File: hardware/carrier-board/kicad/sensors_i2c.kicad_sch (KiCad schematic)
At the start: 0 parts

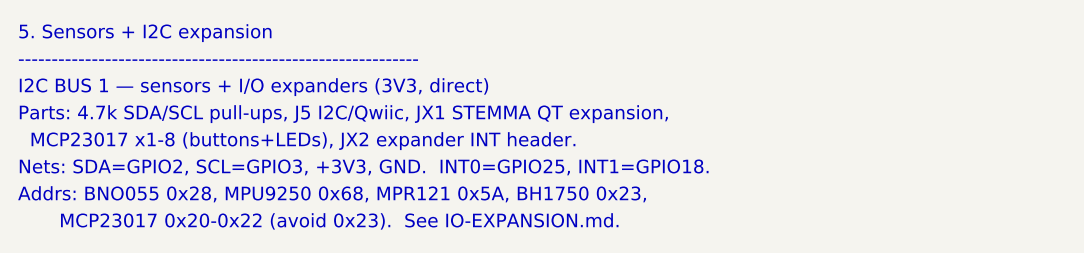
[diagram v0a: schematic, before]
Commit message: Carrier docs + KiCad plan: full two-brain pass (CM5 HUB75 + RP2354B I/O)
Propagate the two-brain architecture across the whole doc set and KiCad plan:
- REQUIREMENTS: restructured M1-M12 (CM5 HUB75; RP2354B core/MAX7219/WS2812/
  sensors/buttons/servos; USB selector + standalone program port); N-list reworked.
- POWER: add +V_SERVO and +3V3_RP rails, servo current budget, updated worked
  total + protection; sensors now on +3V3_RP not CM5 3V3.
- CONNECTORS: J3 re-sourced to RP2354B SPI0, J4 4 WS2812 zones, J5 +SENS_INT,
  J6 BTN1..10, add J12 USB-C, J20-J27 servos, SW1 USB selector, SWD/UART hdrs;
  drop JP1/JP2; fans presented as RP2354B-default-or-CM5 (decision flagged).
- BOM: add RP2354B core, '125/'245 (RP side), USB mux/USB-C/ESD, servo headers,
  +3V3_RP reg; fix '125 double-count and stale HUB75/MAX7219-shared-buffer/JP1.
- MULTI-BACKEND: HUB75+MAX7219 now simultaneous (different brains); firmware
  CompositePanelOutput is the sole remaining blocker.
- IO-EXPANSION: RP2354B is the primary I/O backbone; I2C expanders secondary.
- kicad: 11-sheet plan, stable UUIDs, generator skips populated face_buffer.
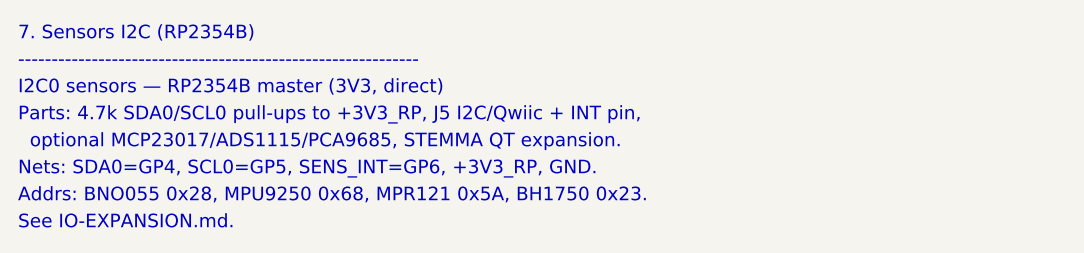
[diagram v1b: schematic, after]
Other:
- note added: "7. Sensors I2C (RP2354B)"
- note added: "Addrs: BNO055 0x28, MPU9250 0x68, MPR121 0x5A, BH1750 0x23."
- note added: "I2C0 sensors — RP2354B master (3V3, direct)"
- note added: "Nets: SDA0=GP4, SCL0=GP5, SENS_INT=GP6, +3V3_RP, GND."
- note added: "Parts: 4.7k SDA0/SCL0 pull-ups to +3V3_RP, J5 I2C/Qwiic + INT pin,"
- note added: "See IO-EXPANSION.md."
- note added: "optional MCP23017/ADS1115/PCA9685, STEMMA QT expansion."
- note removed: "5. Sensors + I2C expansion"
- note removed: "Addrs: BNO055 0x28, MPU9250 0x68, MPR121 0x5A, BH1750 0x23,"
- note removed: "I2C BUS 1 — sensors + I/O expanders (3V3, direct)"
- note removed: "MCP23017 0x20-0x22 (avoid 0x23). See IO-EXPANSION.md."
- note removed: "MCP23017 x1-8 (buttons+LEDs), JX2 expander INT header."
- note removed: "Nets: SDA=GPIO2, SCL=GPIO3, +3V3, GND. INT0=GPIO25, INT1=GPIO18."
- note removed: "Parts: 4.7k SDA/SCL pull-ups, J5 I2C/Qwiic, JX1 STEMMA QT expansion,"
- title: ProtoHUD Carrier — 5. Sensors + I2C expansion -> ProtoHUD Carrier — 7. Sensors I2C (RP2354B)
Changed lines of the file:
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@@
   (paper "A3")
   (title_block
-    (title "ProtoHUD Carrier — 5. Sensors + I2C expansion")
+    (title "ProtoHUD Carrier — 7. Sensors I2C (RP2354B)")
     (rev "A")
     (company "ProtoHUD")
   )
-  (text "5. Sensors + I2C expansion" (at 25.4 25.40 0) (effects (font (size 1.5 1.5)) (justify left bottom)))
+  (text "7. Sensors I2C (RP2354B)" (at 25.4 25.40 0) (effects (font (size 1.5 1.5)) (justify left bottom)))
   (text "------------------------------------------------------------" (at 25.4 28.40 0) (effects (font (size 1.5 1.5)) (justify left bottom)))
-  (text "I2C BUS 1 — sensors + I/O expanders (3V3, direct)" (at 25.4 31.40 0) (effects (font (size 1.5 1.5)) (justify left bottom)))
-  (text "Parts: 4.7k SDA/SCL pull-ups, J5 I2C/Qwiic, JX1 STEMMA QT expansion," (at 25.4 34.40 0) (effects (font (size 1.5 1.5)) (justify left bottom)))
-  (text "  MCP23017 x1-8 (buttons+LEDs), JX2 expander INT header." (at 25.4 37.40 0) (effects (font (size 1.5 1.5)) (justify left bottom)))
-  (text "Nets: SDA=GPIO2, SCL=GPIO3, +3V3, GND.  INT0=GPIO25, INT1=GPIO18." (at 25.4 40.40 0) (effects (font (size 1.5 1.5)) (justify left bottom)))
-  (text "Addrs: BNO055 0x28, MPU9250 0x68, MPR121 0x5A, BH1750 0x23," (at 25.4 43.40 0) (effects (font (size 1.5 1.5)) (justify left bottom)))
-  (text "       MCP23017 0x20-0x22 (avoid 0x23).  See IO-EXPANSION.md." (at 25.4 46.40 0) (effects (font (size 1.5 1.5)) (justify left bottom)))
+  (text "I2C0 sensors — RP2354B master (3V3, direct)" (at 25.4 31.40 0) (effects (font (size 1.5 1.5)) (justify left bottom)))
+  (text "Parts: 4.7k SDA0/SCL0 pull-ups to +3V3_RP, J5 I2C/Qwiic + INT pin," (at 25.4 34.40 0) (effects (font (size 1.5 1.5)) (justify left bottom)))
+  (text "  optional MCP23017/ADS1115/PCA9685, STEMMA QT expansion." (at 25.4 37.40 0) (effects (font (size 1.5 1.5)) (justify left bottom)))
+  (text "Nets: SDA0=GP4, SCL0=GP5, SENS_INT=GP6, +3V3_RP, GND." (at 25.4 40.40 0) (effects (font (size 1.5 1.5)) (justify left bottom)))
+  (text "Addrs: BNO055 0x28, MPU9250 0x68, MPR121 0x5A, BH1750 0x23." (at 25.4 43.40 0) (effects (font (size 1.5 1.5)) (justify left bottom)))
+  (text "See IO-EXPANSION.md." (at 25.4 46.40 0) (effects (font (size 1.5 1.5)) (justify left bottom)))
   (sheet_instances
     (path "/" (page "1"))

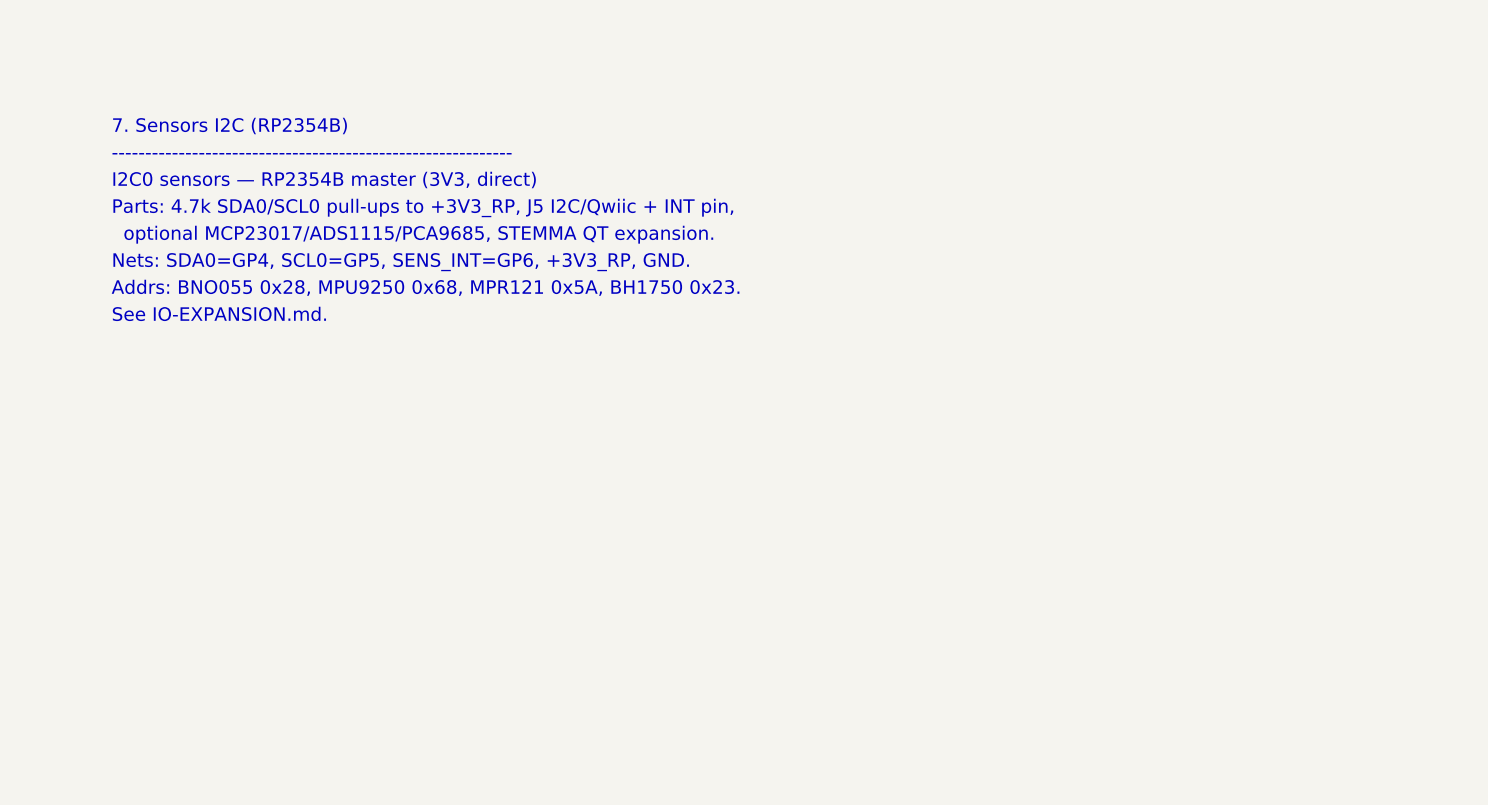
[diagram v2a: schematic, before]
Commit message: Carrier KiCad: populate all 11 schematic sheets
Replace populate_face_buffer.py with populate_sheets.py: one generator that
emits all 11 populated sub-sheets reusing the KiCad-9 format proven by the
face_buffer proof. Shared symbol library + generic box-symbol builder; condensed
CM5 (2x DF40-100) and RP2354B (QFN-80) symbols showing only used pins.

Connectivity by net labels (global for rails + cross-sheet nets: GPIOxx HUB75,
MX_*, LED*_DAT, SRV*, BTN*, *_USB_*; local within-sheet). Sheets: power
(protection + rails + AP2112 +3V3_RP), cm5 (HUB75 out + fan MOSFETs + RP ctrl),
face_buffer, rp2354_io (RP2354B + xtal + SW1/J12 + ESD + SWD), rp2354_face
(U10->J3), leds (U11 quad ->J4a-d), sensors_i2c (pull-ups+J5+STEMMA),
servos (J20-27 + rail), gpio_buttons (J6), usb (USB2514B hub + uplink),
cameras_display (CSI FFC + HDMI).

Verified: all sheets paren-balanced, every used lib_id defined, all instance
paths match sheet UUIDs, root<->sub-sheet UUID linkage intact. generate_skeleton.py
now lists all sheets POPULATED (writes only root+project). Not yet opened in
KiCad here -- expect ERC warnings (PWR_FLAG, unconnected pins) to clean.
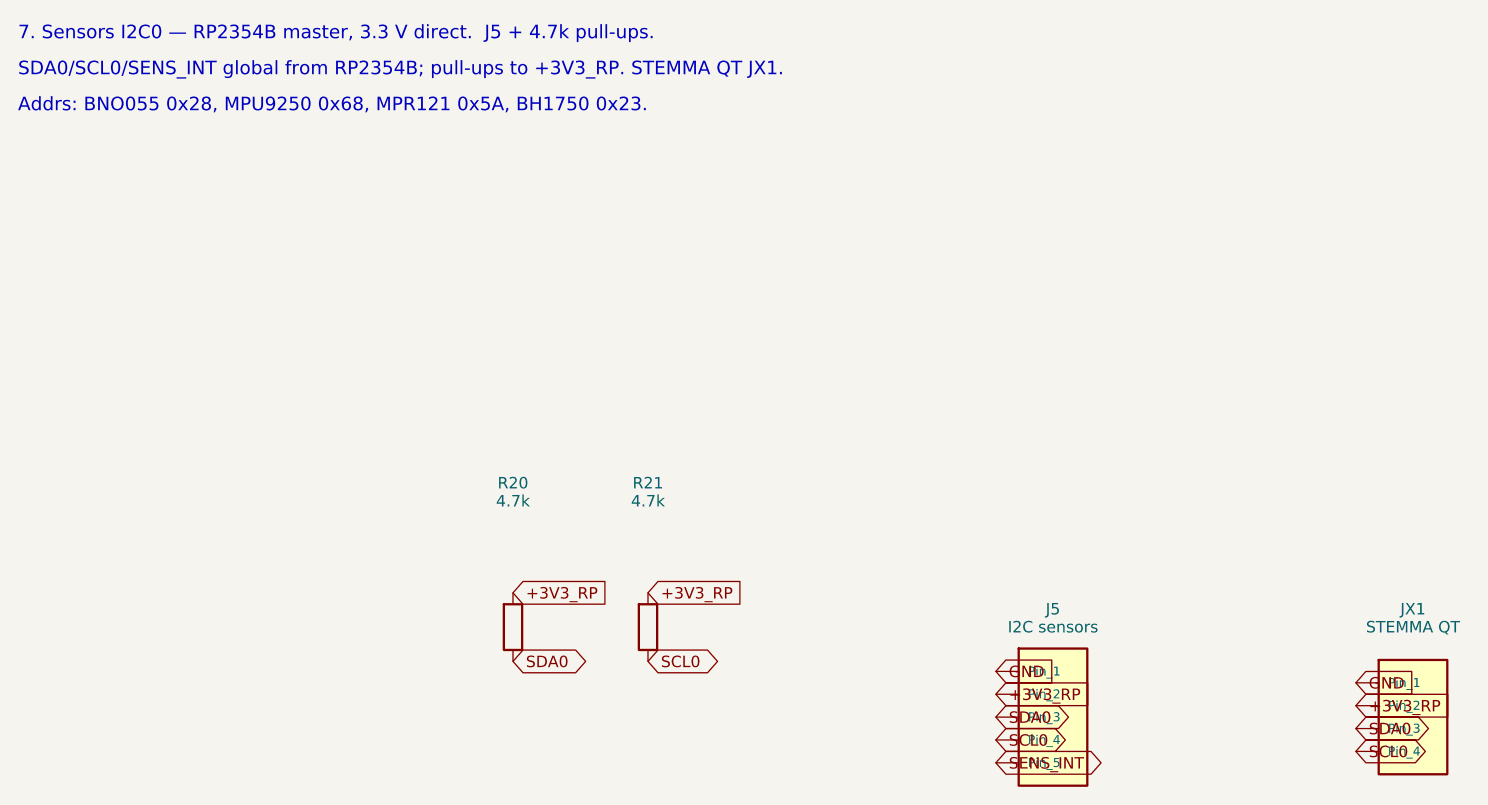
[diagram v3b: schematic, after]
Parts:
- added J5: I2C sensors, symbol Connector_Generic:Conn_01x05
- added JX1: STEMMA QT, symbol Connector_Generic:Conn_01x04
- added R20, R21: 4.7k, symbol Device:R
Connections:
- new net +3V3_RP: J5.2 (Pin_2), JX1.2 (Pin_2), R20.1, R21.1
- new net GND: J5.1 (Pin_1), JX1.1 (Pin_1)
- new net SCL0: J5.4 (Pin_4), JX1.4 (Pin_4), R21.2
- new net SDA0: J5.3 (Pin_3), JX1.3 (Pin_3), R20.2
- new net SENS_INT: J5.5 (Pin_5)
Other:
- note added: "7. Sensors I2C0 — RP2354B master, 3.3 V direct. J5 + 4.7k pull-ups."
- note added: "SDA0/SCL0/SENS_INT global from RP2354B; pull-ups to +3V3_RP. STEMMA QT JX1."
- note removed: "------------------------------------------------------------"
- note removed: "7. Sensors I2C (RP2354B)"
- note removed: "I2C0 sensors — RP2354B master (3V3, direct)"
- note removed: "Nets: SDA0=GP4, SCL0=GP5, SENS_INT=GP6, +3V3_RP, GND."
- note removed: "Parts: 4.7k SDA0/SCL0 pull-ups to +3V3_RP, J5 I2C/Qwiic + INT pin,"
- note removed: "See IO-EXPANSION.md."
- note removed: "optional MCP23017/ADS1115/PCA9685, STEMMA QT expansion."
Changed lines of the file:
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@@
 (kicad_sch
-  (version 20230121)
-  (generator protohud_skeleton)
+  (version 20250114)
+  (generator "protohud_populate")
+  (generator_version "9.0")
   (paper "A3")
   (title_block
@@
     (company "ProtoHUD")
   )
-  (text "7. Sensors I2C (RP2354B)" (at 25.4 25.40 0) (effects (font (size 1.5 1.5)) (justify left bottom)))
-  (text "------------------------------------------------------------" (at 25.4 28.40 0) (effects (font (size 1.5 1.5)) (justify left bottom)))
-  (text "I2C0 sensors — RP2354B master (3V3, direct)" (at 25.4 31.40 0) (effects (font (size 1.5 1.5)) (justify left bottom)))
-  (text "Parts: 4.7k SDA0/SCL0 pull-ups to +3V3_RP, J5 I2C/Qwiic + INT pin," (at 25.4 34.40 0) (effects (font (size 1.5 1.5)) (justify left bottom)))
-  (text "  optional MCP23017/ADS1115/PCA9685, STEMMA QT expansion." (at 25.4 37.40 0) (effects (font (size 1.5 1.5)) (justify left bottom)))
-  (text "Nets: SDA0=GP4, SCL0=GP5, SENS_INT=GP6, +3V3_RP, GND." (at 25.4 40.40 0) (effects (font (size 1.5 1.5)) (justify left bottom)))
-  (text "Addrs: BNO055 0x28, MPU9250 0x68, MPR121 0x5A, BH1750 0x23." (at 25.4 43.40 0) (effects (font (size 1.5 1.5)) (justify left bottom)))
-  (text "See IO-EXPANSION.md." (at 25.4 46.40 0) (effects (font (size 1.5 1.5)) (justify left bottom)))
+  (text "7. Sensors I2C0 — RP2354B master, 3.3 V direct.  J5 + 4.7k pull-ups." (at 15 15.0 0) (effects (font (size 1.5 1.5)) (justify left bottom)))
+  (text "SDA0/SCL0/SENS_INT global from RP2354B; pull-ups to +3V3_RP. STEMMA QT JX1." (at 15 19.0 0) (effects (font (size 1.5 1.5)) (justify left bottom)))
+  (text "Addrs: BNO055 0x28, MPU9250 0x68, MPR121 0x5A, BH1750 0x23." (at 15 23.0 0) (effects (font (size 1.5 1.5)) (justify left bottom)))
+  (symbol
+    (lib_id "Device:R")
+    (at 70.00 80.00 0)
+    (unit 1)
+    (exclude_from_sim no) (in_bom yes) (on_board yes) (dnp no)
+    (property "Reference" "R20" (at 70.00 64.00 0) (effects (font (size 1.27 1.27))))
+    (property "Value" "4.7k" (at 70.00 66.00 0) (effects (font (size 1.27 1.27))))
+    (property "Footprint" "" (at 70.00 80.00 0) (effects (font (size 1.27 1.27)) (hide yes)))
+    (property "Datasheet" "" (at 70.00 80.00 0) (effects (font (size 1.27 1.27)) (hide yes)))
+    (pin "1")
+    (pin "2")
+    (instances
+      (project "ProtoHUD-Carrier"
+        (path "/aa17a73e-e56b-4b1f-a092-064b3bde23cb"
+          (reference "R20") (unit 1))))
+  )
+  (symbol
+    (lib_id "Device:R")
+    (at 85.00 80.00 0)
+    (unit 1)
+    (exclude_from_sim no) (in_bom yes) (on_board yes) (dnp no)
+    (property "Reference" "R21" (at 85.00 64.00 0) (effects (font (size 1.27 1.27))))
+    (property "Value" "4.7k" (at 85.00 66.00 0) (effects (font (size 1.27 1.27))))
+    (property "Footprint" "" (at 85.00 80.00 0) (effects (font (size 1.27 1.27)) (hide yes)))
+    (property "Datasheet" "" (at 85.00 80.00 0) (effects (font (size 1.27 1.27)) (hide yes)))
+    (pin "1")
+    (pin "2")
+    (instances
+      (project "ProtoHUD-Carrier"
+        (path "/aa17a73e-e56b-4b1f-a092-064b3bde23cb"
+          (reference "R21") (unit 1))))
+  )
+  (symbol
+    (lib_id "Connector_Generic:Conn_01x05")
+    (at 130.00 90.00 0)
+    (unit 1)
+    (exclude_from_sim no) (in_bom yes) (on_board yes) (dnp no)
+    (property "Reference" "J5" (at 130.00 78.00 0) (effects (font (size 1.27 1.27))))
+    (property "Value" "I2C sensors" (at 130.00 80.00 0) (effects (font (size 1.27 1.27))))
+    (property "Footprint" "" (at 130.00 90.00 0) (effects (font (size 1.27 1.27)) (hide yes)))
+    (property "Datasheet" "" (at 130.00 90.00 0) (effects (font (size 1.27 1.27)) (hide yes)))
+    (pin "1")
+    (pin "2")
+    (pin "3")
+    (pin "4")
+    (pin "5")
+    (instances
+      (project "ProtoHUD-Carrier"
+        (path "/aa17a73e-e56b-4b1f-a092-064b3bde23cb"
+          (reference "J5") (unit 1))))
+  )
+  (symbol
+    (lib_id "Connector_Generic:Conn_01x04")
+    (at 170.00 90.00 0)
+    (unit 1)
+    (exclude_from_sim no) (in_bom yes) (on_board yes) (dnp no)
+    (property "Reference" "JX1" (at 170.00 78.00 0) (effects (font (size 1.27 1.27))))
+    (property "Value" "STEMMA QT" (at 170.00 80.00 0) (effects (font (size 1.27 1.27))))
+    (property "Footprint" "" (at 170.00 90.00 0) (effects (font (size 1.27 1.27)) (hide yes)))
+    (property "Datasheet" "" (at 170.00 90.00 0) (effects (font (size 1.27 1.27)) (hide yes)))
+    (pin "1")
+    (pin "2")
+    (pin "3")
+    (pin "4")
+    (instances
+      (project "ProtoHUD-Carrier"
+        (path "/aa17a73e-e56b-4b1f-a092-064b3bde23cb"
+          (reference "JX1") (unit 1))))
+  )
+  (global_label "+3V3_RP" (shape input) (at 70.00 76.19 0) (effects (font (size 1.27 1.27)) (justify left)))
+  (global_label "SDA0" (shape bidirectional) (at 70.00 83.81 0) (effects (font (size 1.27 1.27)) (justify left)))
+  (global_label "+3V3_RP" (shape input) (at 85.00 76.19 0) (effects (font (size 1.27 1.27)) (justify left)))
+  (global_label "SCL0" (shape bidirectional) (at 85.00 83.81 0) (effects (font (size 1.27 1.27)) (justify left)))
+  (global_label "GND" (shape input) (at 123.65 84.92 180) (effects (font (size 1.27 1.27)) (justify left)))
+  (global_label "+3V3_RP" (shape input) (at 123.65 87.46 180) (effects (font (size 1.27 1.27)) (justify left)))
+  (global_label "SDA0" (shape bidirectional) (at 123.65 90.00 180) (effects (font (size 1.27 1.27)) (justify left)))
+  (global_label "SCL0" (shape bidirectional) (at 123.65 92.54 180) (effects (font (size 1.27 1.27)) (justify left)))
+  (global_label "SENS_INT" (shape bidirectional) (at 123.65 95.08 180) (effects (font (size 1.27 1.27)) (justify left)))
+  (global_label "GND" (shape input) (at 163.65 86.19 180) (effects (font (size 1.27 1.27)) (justify left)))
+  (global_label "+3V3_RP" (shape input) (at 163.65 88.73 180) (effects (font (size 1.27 1.27)) (justify left)))
+  (global_label "SDA0" (shape bidirectional) (at 163.65 91.27 180) (effects (font (size 1.27 1.27)) (justify left)))
+  (global_label "SCL0" (shape bidirectional) (at 163.65 93.81 180) (effects (font (size 1.27 1.27)) (justify left)))
   (sheet_instances
     (path "/" (page "1"))
